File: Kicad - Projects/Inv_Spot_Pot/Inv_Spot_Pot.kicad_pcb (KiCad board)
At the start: 2 copper layers, 189.9 x 126.8 mm, 72 parts, among them J1 Screw_Terminal_01x03, J2 PWM, J3 Display_Power, J4 Current_Sense, J5 PWM, Q1 40T120, Q2 40T120, Q3 40T120, Q4 40T120, T1 Transformer_1P_2S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

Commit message: Adicionados Testpoints
Adicionados testpoints:
 - Gate de cada IGBT (+ emissor)
 - Tensão do barramento
 - Barramento da fonte auxiliar

Trocado footprint do sensor de corrente para pinheader
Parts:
- J4: footprint Connector_JST:JST_ZH_B2B-ZR_1x02_P1.50mm_Vertical -> Connector_PinHeader_2.00mm:PinHeader_1x02_P2.00mm_Vertical
- turned J4 to 90 degrees
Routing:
- net ~{Gate}: track 12.8 -> 18.1 mm, vias 0 -> 1
- net Earth: vias 1 -> 3
- net Net-(T1-AB): vias 0 -> 1
- net ~{Gate1}: vias 0 -> 1
- net T-: vias 4 -> 6
- net T+: vias 0 -> 1
- net Gate1: vias 0 -> 1
- net Gate: vias 0 -> 1
- net 310V: vias 0 -> 1

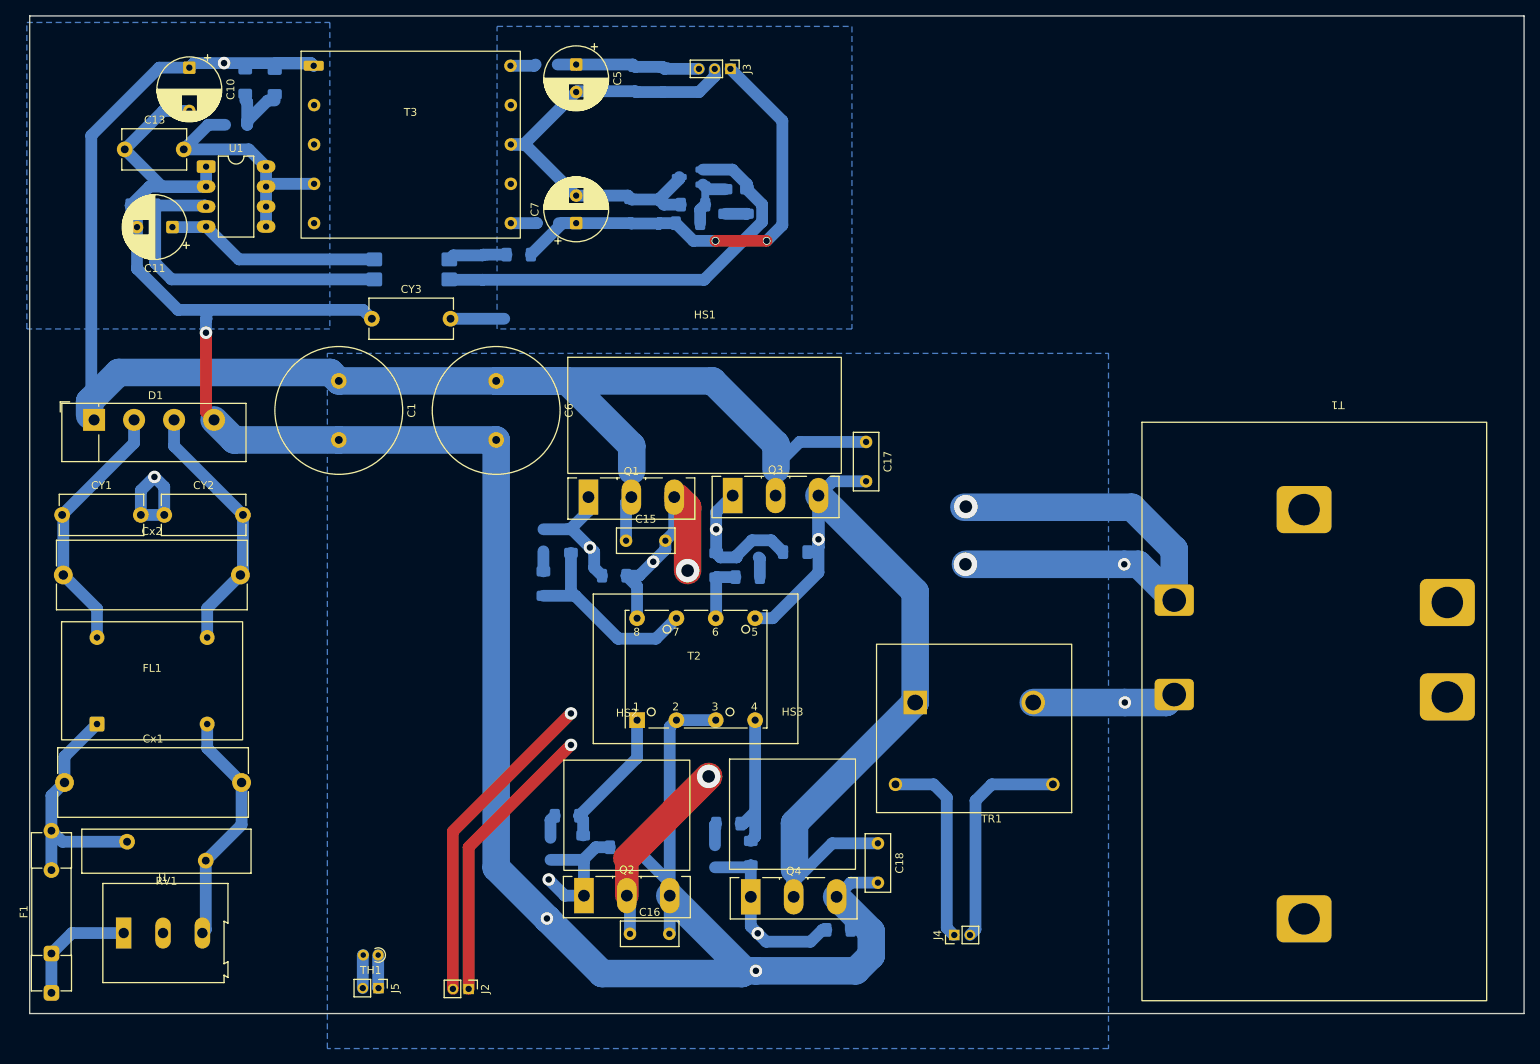
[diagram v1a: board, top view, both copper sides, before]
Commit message: Finalizada Placa de Potência
Capacitor de desacoplamento de 15V da fonte auxiliar movido para estar mais próximo da saída

Footprint do transformador corrigida

PWM da camada de cima afastado do dissipador de Q2

Maior afastamento entre planos GND/Earth e trilhas na fonte auxiliar

Modificado símbolo do transformador de saída no esquemático para melhor refletir a saída
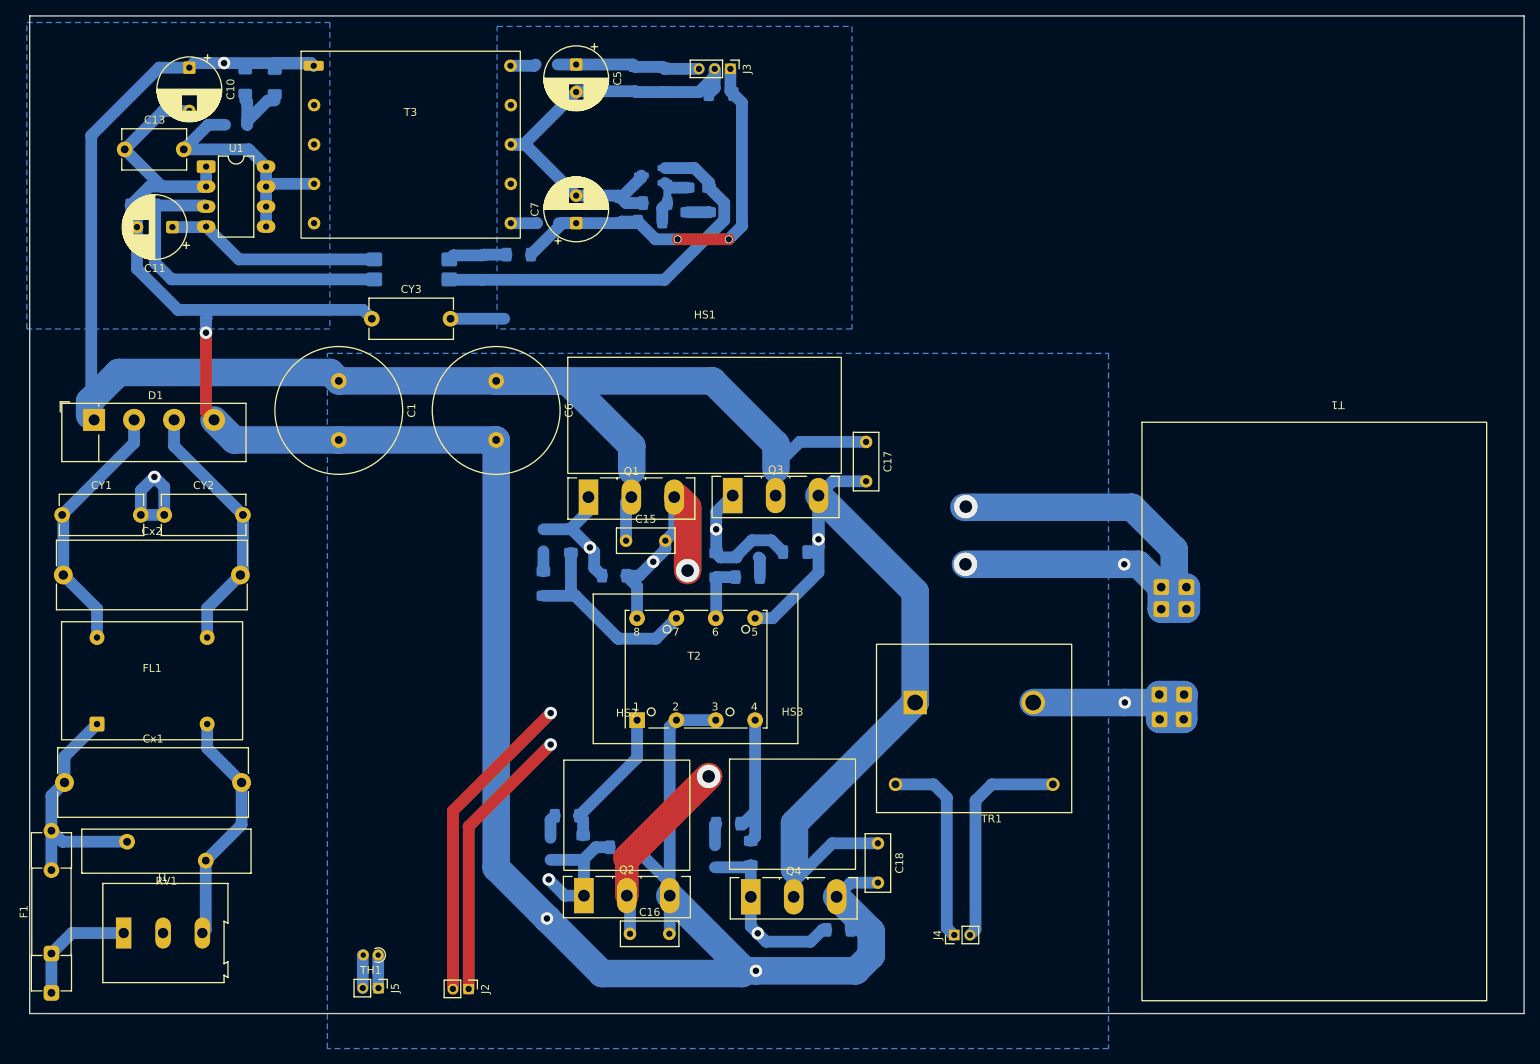
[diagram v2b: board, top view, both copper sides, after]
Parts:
- moved C9 18.8 mm to (121.0, 40.0), turned to 180 degrees
- moved C4 4.82 mm to (116.8, 53.4)
- moved R10 4.82 mm to (112.7, 53.8)
- moved R11 4.82 mm to (112.0, 56.2)
- moved R15 4.82 mm to (108.3, 54.7)
- moved R9 4.82 mm to (119.5, 53.4)
- moved U3 4.82 mm to (112.4, 50.3)
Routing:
- net Net-(T1-AB): track 18.3 -> 30.9 mm
- net T-: track 117.5 -> 129.5 mm
- net 15V: track 60.2 -> 55.2 mm
- net Net-(U3-K): track 54.8 -> 50.0 mm
- net GND: track 66.0 -> 64.7 mm
- net /PWM_L: track 41.2 -> 40.2 mm
- net /PWM_H: track 36.4 -> 35.4 mm

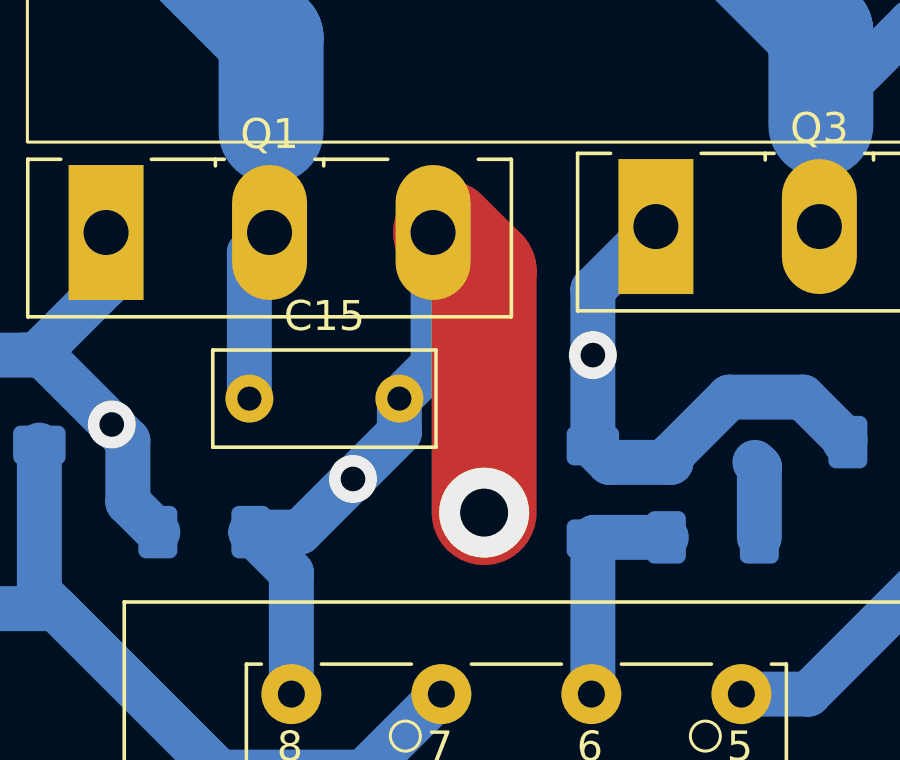
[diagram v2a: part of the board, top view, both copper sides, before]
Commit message: Ajustes de Esquemático - Display
Feito:
 - Ajustes genéricos para melhor legibilidade
 - Implementado Opto para leitura do gatilho (com pull-up no lado do uC)
 - Trocados footprints das conexões para pinheader
 - Ajuste na trilha T- do IGBT superior

À fazer:
 - Trocar todos os resistores por SMD
 - Revisar com Anderson sobre topologias/conectores
 - Revisar com Anderson sobre afastamento do plano de referência da trilha "Earth" dos IGBTs inferiores
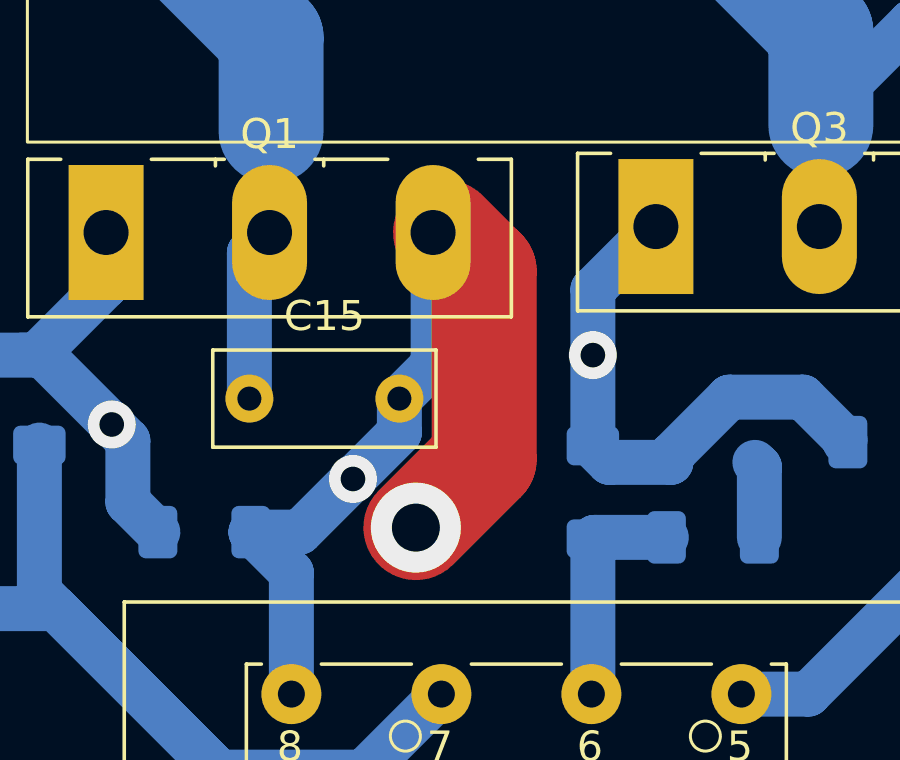
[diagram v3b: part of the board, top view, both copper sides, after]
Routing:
- net T-: track 129.5 -> 131.0 mm
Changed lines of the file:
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@@
 	)
 	(segment
-		(start 116.775 92.45)
-		(end 116.775 100.5)
+		(start 114.5 101)
+		(end 116.775 98.725)
 		(width 3.5)
 		(layer "F.Cu")
@@
 	)
 	(segment
-		(start 115.488019 91.163019)
+		(start 116.775 98.725)
 		(end 116.775 92.45)
 		(width 3.5)
@@
 		(end 109.05 137.05)
 		(width 3)
+		(layer "F.Cu")
+		(net "T-")
+	)
+	(segment
+		(start 116.775 92.45)
+		(end 115.488019 91.163019)
+		(width 3.5)
 		(layer "F.Cu")
 		(net "T-")
@@
 	)
 	(via
-		(at 116.775 100.5)
+		(at 114.5 101)
 		(size 3)
 		(drill 1.6)

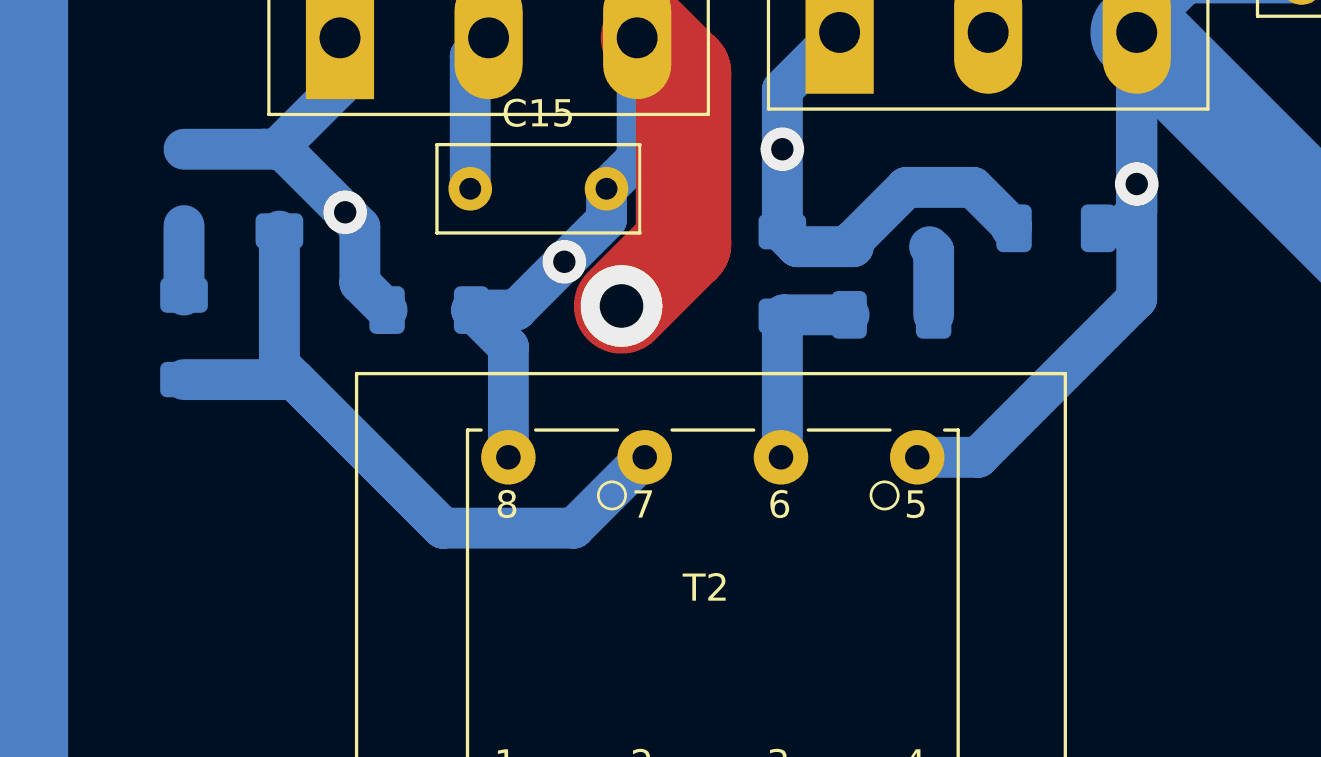
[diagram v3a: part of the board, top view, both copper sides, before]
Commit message: Primeiro Layout - Display
Feito o layout preliminar da placa de display, conferir com o Anderson

Corrigido problema com o layout do transformador (erro no símbolo utilizado levou a inversão dos IGBTs superiores)
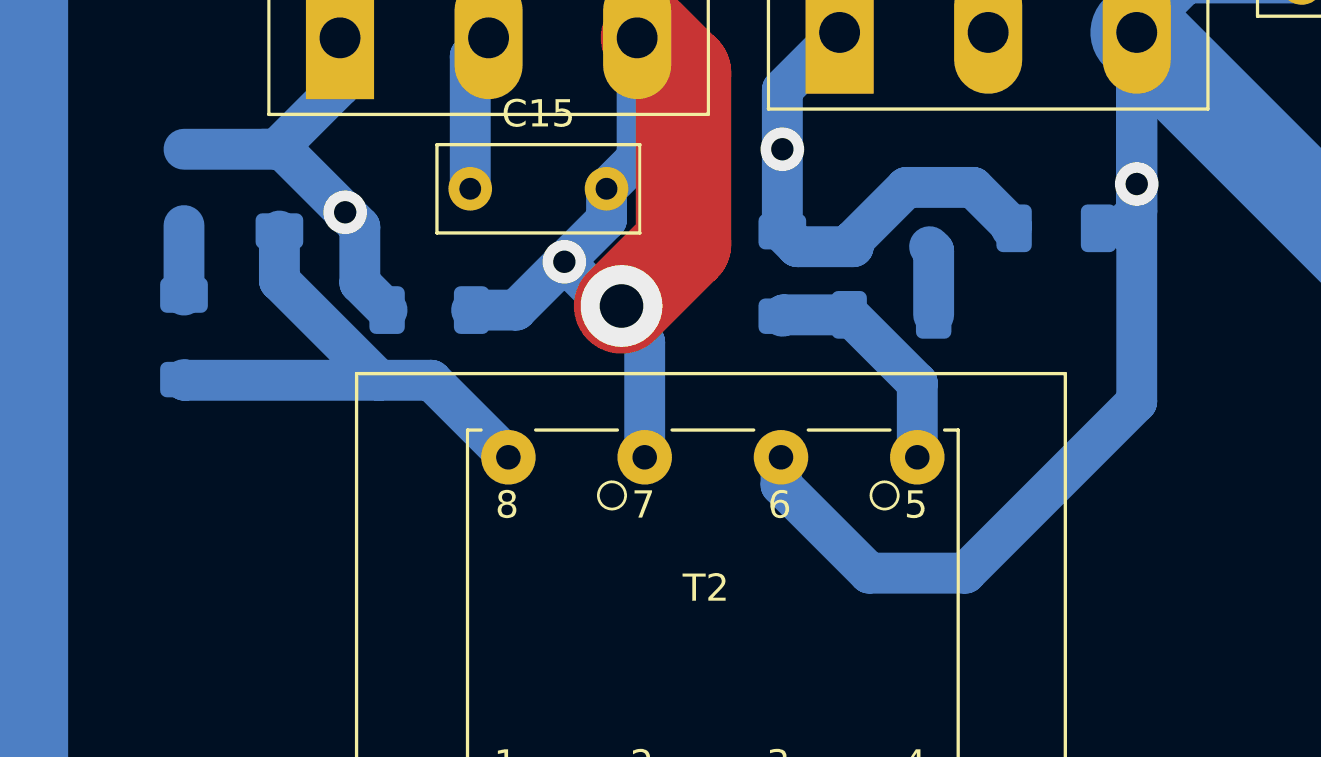
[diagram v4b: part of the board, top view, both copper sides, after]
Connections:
- T2 pad 5: T+ -> PWM1
- T2 pad 6: PWM1 -> T+
- T2 pad 7: PWM -> T-
- T2 pad 8: T- -> PWM
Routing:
- net PWM: track 33.6 -> 20.1 mm
- net T+: track 111.5 -> 122.9 mm
- net T-: track 131.0 -> 133.4 mm
- net PWM1: track 7.67 -> 8.73 mm
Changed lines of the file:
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@@
 			(unit
 				(name "A")
-				(pins "4" "3" "2" "1" "7" "8" "5" "6")
+				(pins "4" "3" "2" "1" "8" "7" "6" "5")
 			)
 		)
@@
 			(layers "*.Cu" "*.Mask")
 			(remove_unused_layers no)
-			(net "T+")
+			(net "PWM1")
 			(pintype "passive")
 		)
@@
 			(layers "*.Cu" "*.Mask")
 			(remove_unused_layers no)
-			(net "PWM1")
+			(net "T+")
 			(pintype "passive")
 		)
@@
 			(layers "*.Cu" "*.Mask")
 			(remove_unused_layers no)
-			(net "PWM")
+			(net "T-")
 			(pintype "passive")
 		)
@@
 			(layers "*.Cu" "*.Mask")
 			(remove_unused_layers no)
-			(net "T-")
+			(net "PWM")
 			(pintype "passive")
 		)
@@
 	)
 	(segment
-		(start 110.35 106.55)
-		(end 110.35 102.5)
-		(width 1.5)
-		(layer "B.Cu")
-		(net "T-")
-	)
-	(segment
 		(start 178.6 97.825)
 		(end 173.225 92.45)
@@
 	)
 	(segment
+		(start 115.35 106.55)
+		(end 115.35 102.325)
+		(width 1.5)
+		(layer "B.Cu")
+		(net "T-")
+	)
+	(segment
 		(start 113.95 97.83137)
 		(end 112.403185 99.378185)
@@
 	)
 	(segment
-		(start 110.35 102.5)
-		(end 109 101.15)
-		(width 1.5)
-		(layer "B.Cu")
-		(net "T-")
-	)
-	(segment
 		(start 113.95 96.7)
 		(end 113.95 97.83137)
@@
 	)
 	(segment
+		(start 115.35 102.325)
+		(end 112.403185 99.378185)
+		(width 1.5)
+		(layer "B.Cu")
+		(net "T-")
+	)
+	(segment
 		(start 112.403185 99.378185)
 		(end 110.63137 101.15)
@@
 	)
 	(segment
-		(start 125.35 106.55)
-		(end 127.581674 106.55)
+		(start 120.35 107.560408)
+		(end 123.589592 110.8)
+		(width 1.5)
+		(layer "B.Cu")
+		(net "T+")
+	)
+	(segment
+		(start 133.4 104.510408)
+		(end 133.4 96.525)
+		(width 1.5)
+		(layer "B.Cu")
+		(net "T+")
+	)
+	(segment
+		(start 127.110408 110.8)
+		(end 133.4 104.510408)
 		(width 1.5)
 		(layer "B.Cu")
@@
 	)
 	(segment
-		(start 133.4 100.731674)
-		(end 133.4 96.525)
+		(start 139.45 89.15)
+		(end 135.215 89.15)
 		(width 1.5)
 		(layer "B.Cu")
@@
 	)
 	(segment
-		(start 139.45 89.15)
-		(end 135.215 89.15)
+		(start 123.589592 110.8)
+		(end 127.110408 110.8)
 		(width 1.5)
 		(layer "B.Cu")
@@
 	)
 	(segment
-		(start 127.581674 106.55)
-		(end 133.4 100.731674)
+		(start 120.35 106.55)
+		(end 120.35 107.560408)
 		(width 1.5)
 		(layer "B.Cu")
@@
 	)
 	(segment
-		(start 120.4 101.375)
-		(end 120.4 106.5)
+		(start 125.35 103.825)
+		(end 122.85 101.325)
 		(width 1.5)
 		(layer "B.Cu")
@@
 	)
 	(segment
-		(start 120.45 101.325)
-		(end 120.4 101.375)
+		(start 125.35 106.55)
+		(end 125.35 103.825)
 		(width 1.5)
 		(layer "B.Cu")
@@
 	)
 	(segment
-		(start 122.85 101.325)
-		(end 120.45 101.325)
+		(start 120.45 101.325)
+		(end 120.4 101.375)
 		(width 1.5)
 		(layer "B.Cu")
@@
 	)
 	(segment
-		(start 120.4 106.5)
-		(end 120.35 106.55)
+		(start 122.85 101.325)
+		(end 120.45 101.325)
 		(width 1.5)
 		(layer "B.Cu")
@@
 	)
 	(segment
-		(start 102.5 103.7)
-		(end 107.95 109.15)
+		(start 107.525 103.725)
+		(end 105.604594 103.725)
 		(width 1.5)
 		(layer "B.Cu")
@@
 	)
 	(segment
-		(start 112.75 109.15)
-		(end 107.95 109.15)
+		(start 101.95 98.25)
+		(end 101.95 100.070406)
 		(width 1.5)
 		(layer "B.Cu")
@@
 	)
 	(segment
-		(start 107.95 109.15)
-		(end 101.95 103.15)
+		(start 110.35 106.55)
+		(end 107.525 103.725)
 		(width 1.5)
 		(layer "B.Cu")
@@
 	)
 	(segment
-		(start 98.45 103.7)
-		(end 102.5 103.7)
+		(start 101.95 100.070406)
+		(end 105.604594 103.725)
 		(width 1.5)
 		(layer "B.Cu")
@@
 	)
 	(segment
-		(start 115.35 106.55)
-		(end 112.75 109.15)
+		(start 98.475 103.725)
+		(end 98.45 103.7)
 		(width 1.5)
 		(layer "B.Cu")
@@
 	)
 	(segment
-		(start 101.95 103.15)
-		(end 101.95 98.25)
+		(start 105.604594 103.725)
+		(end 98.475 103.725)
 		(width 1.5)
 		(layer "B.Cu")
